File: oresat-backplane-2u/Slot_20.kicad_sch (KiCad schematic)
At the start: 10 parts

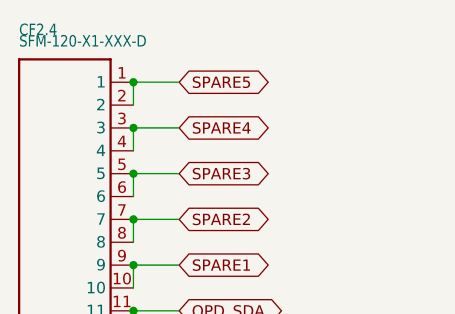
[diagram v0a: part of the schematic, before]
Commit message: Aligned everything to the DXF, should maybe be done I think
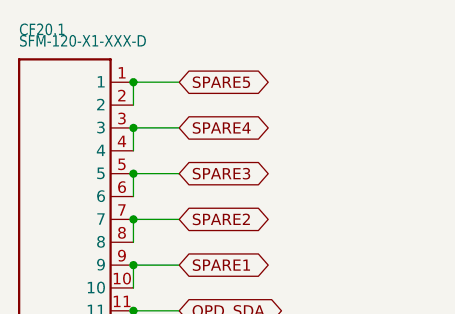
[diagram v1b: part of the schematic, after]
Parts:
- CF20.1: renamed from CF2.4; footprint oresat-backplane-2u:SFM-120-X1-XXX-D -> oresat-footprints:J-SAMTEC-SFM-120-X1-XXX-D
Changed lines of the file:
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@@
   (symbol (lib_id "oresat-backplane-2u-eagle-import:SFM-120-X1-XXX-D") (at 33.02 157.48 0) (unit 1)
     (in_bom yes) (on_board yes)
-    (property "Reference" "CF2.4" (id 0) (at 30.48 106.68 0)
+    (property "Reference" "CF20.1" (id 0) (at 30.48 106.68 0)
       (effects (font (size 1.27 1.0795)) (justify left bottom))
     )
@@
       (effects (font (size 1.27 1.0795)) (justify left bottom))
     )
-    (property "Footprint" "oresat-backplane-2u:SFM-120-X1-XXX-D" (id 2) (at 33.02 157.48 0)
+    (property "Footprint" "oresat-footprints:J-SAMTEC-SFM-120-X1-XXX-D" (id 2) (at 33.02 157.48 0)
       (effects (font (size 1.27 1.27)) hide)
     )
